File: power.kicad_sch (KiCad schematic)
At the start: 46 parts, among them Q1 CSD18511Q5A, Q2 CSD18511Q5A, Q3 CSD18511Q5A, Q4 CSD18511Q5A, U1 LM25119PSQ/NOPB, U2 DS4432U+, U3 INA260

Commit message: added gerbers and BOM
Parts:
- C1, C3, C4: PARTNO (none) -> 35SVPF82M
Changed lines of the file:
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@@
+			)
+		)
+		(property "PARTNO" "35SVPF82M"
+			(at 57.15 87.63 0)
+			(effects
+				(font
+					(size 1.27 1.27)
+				)
+				(hide yes)
 			)
 		)
@@
 			)
 		)
+		(property "PARTNO" "35SVPF82M"
+			(at 44.45 87.63 0)
+			(effects
+				(font
+					(size 1.27 1.27)
+				)
+				(hide yes)
+			)
+		)
 		(pin "1"
 		)
@@
 			(at 69.85 87.63 0)
 			(effects
+				(font
+					(size 1.27 1.27)
+				)
+				(hide yes)
+			)
+		)
+		(property "PARTNO" "35SVPF82M"
+			(at 69.85 87.63 0)
+			(effects

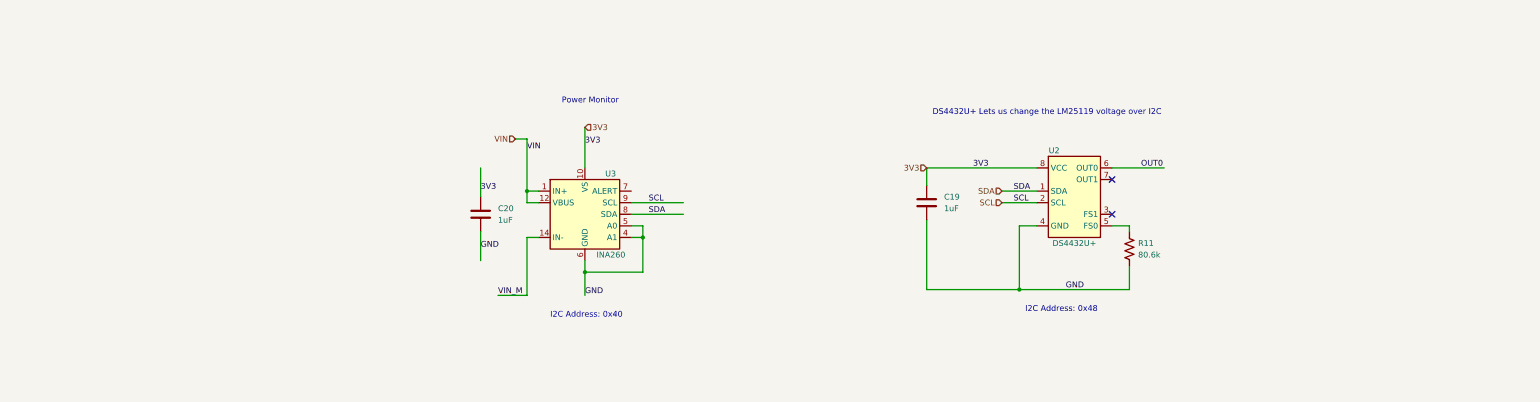
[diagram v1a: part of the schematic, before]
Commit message: added all the ASICs to the schematic. added the RP2040 circuit for data. added the VDDIO boost circuit. schematic cleanup
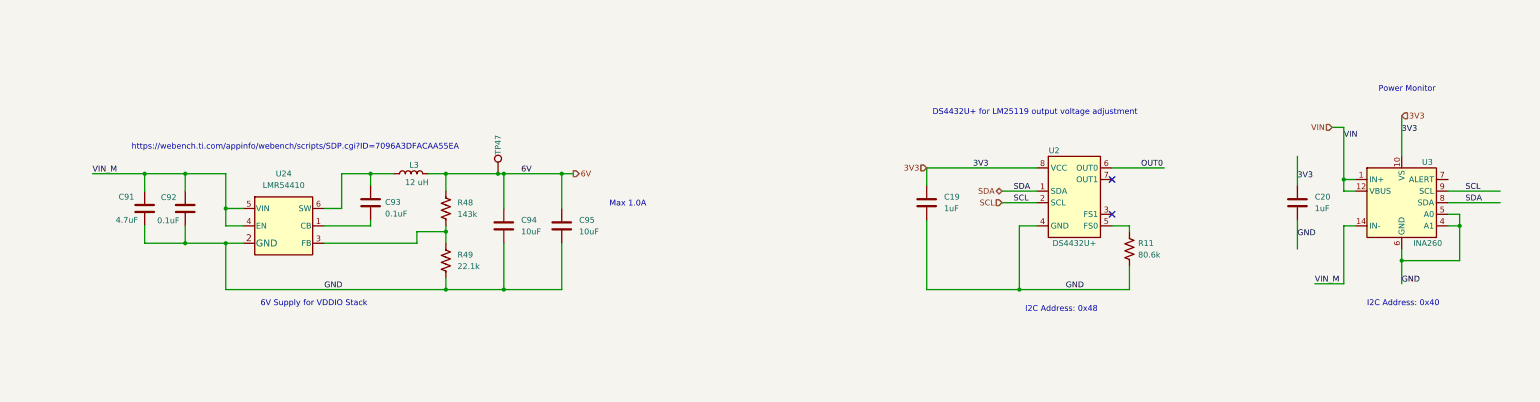
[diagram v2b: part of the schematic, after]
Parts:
- added C91: 4.7uF, Capacitor_SMD:C_0805_2012Metric, symbol Device:C
- added C92: 0.1uF, Capacitor_SMD:C_0603_1608Metric, symbol Device:C
- added C93: 0.1uF, Capacitor_SMD:C_0402_1005Metric, symbol Device:C
- added C94, C95: 10uF, Capacitor_SMD:C_0805_2012Metric, symbol Device:C
- added L3: 12 uH, bitaxe:74438357082, symbol Device:L
- added R48: 143k, Resistor_SMD:R_0402_1005Metric, symbol Device:R_US
- added R49: 22.1k, Resistor_SMD:R_0402_1005Metric, symbol Device:R_US
- added TP47: TestPoint, TestPoint:TestPoint_Pad_D1.0mm, symbol Connector:TestPoint
- added U24: LMR54410, Package_TO_SOT_SMD:SOT-23-6, symbol bitaxe:LMR54410
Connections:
- net GND: now also C91.2, C92.1, C94.2, C95.2, R49.2, U24.2 (GND)
- net VIN_M: now also C91.1, C92.2, U24.4 (EN), U24.5 (VIN)
- new net: C93.2, U24.1 (CB)
- new net: R48.2, R49.1, U24.3 (FB)
- new net: C93.1, L3.1, U24.6 (SW)
- new net 6V: C94.1, C95.1, L3.2, R48.1, TP47.1
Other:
- note added: "6V Supply for VDDIO Stack"
- note added: "DS4432U+ for LM25119 output voltage adjustment"
- note added: "Max 1.0A"
- note added: "https://webench.ti.com/appinfo/webench/scripts/SDP.cgi?ID=7096A3DFACAA55EA"
- note removed: "DS4432U+ Lets us change the LM25119 voltage over I2C"
- moved on the sheet: C20, U3

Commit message: starting layout
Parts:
- L3: footprint bitaxe:74438357082 -> emberone:74438357082
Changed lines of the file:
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@@
 			)
 		)
-		(property "Footprint" "bitaxe:74438357082"
+		(property "Footprint" "emberone:74438357082"
 			(at 138.43 203.2 0)
 			(effects

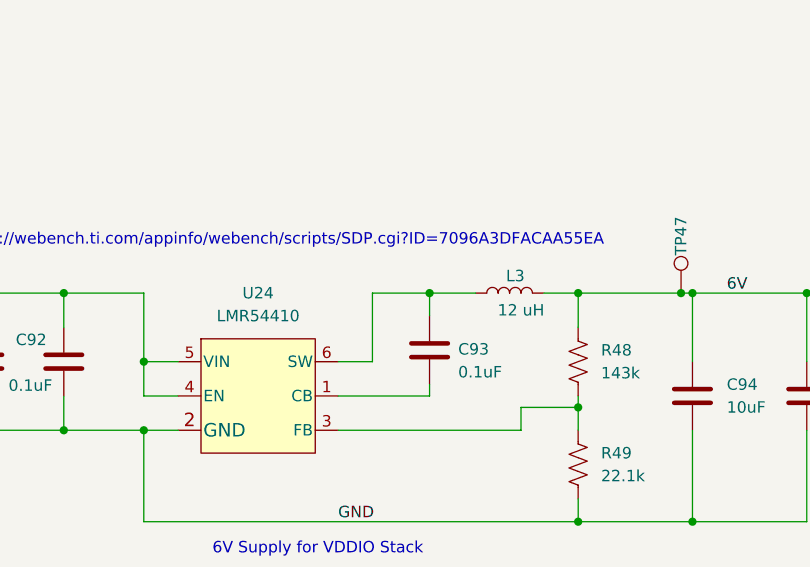
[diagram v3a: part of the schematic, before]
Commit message: moved all the clearance issue passives to the back side and mostly re-routed
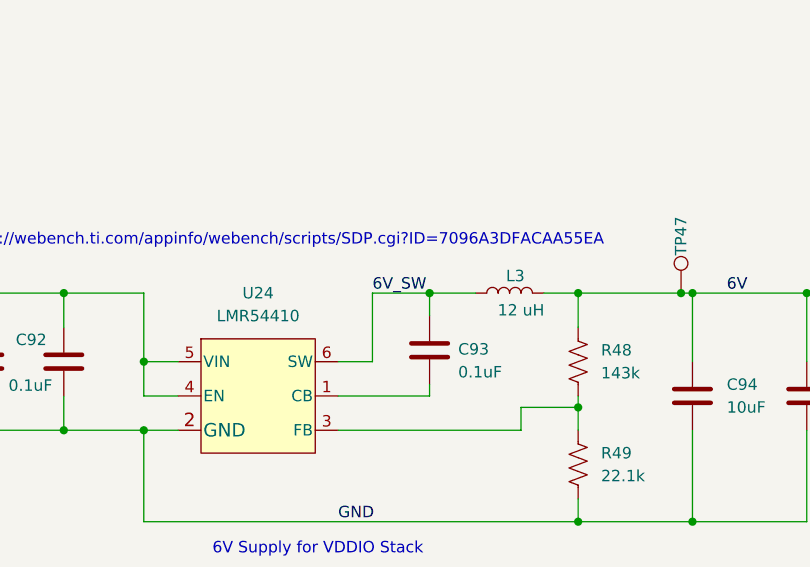
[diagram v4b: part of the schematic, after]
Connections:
- net 6V_SW: now reaches C93.1, L3.1, U24.6 (SW)
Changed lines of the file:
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@@
+		)
+	)
+	(label "6V_SW"
+		(at 123.19 203.2 0)
+		(fields_autoplaced yes)
+		(effects
+			(font
+				(size 1.27 1.27)
+			)
+			(justify left bottom)
 		)
 	)

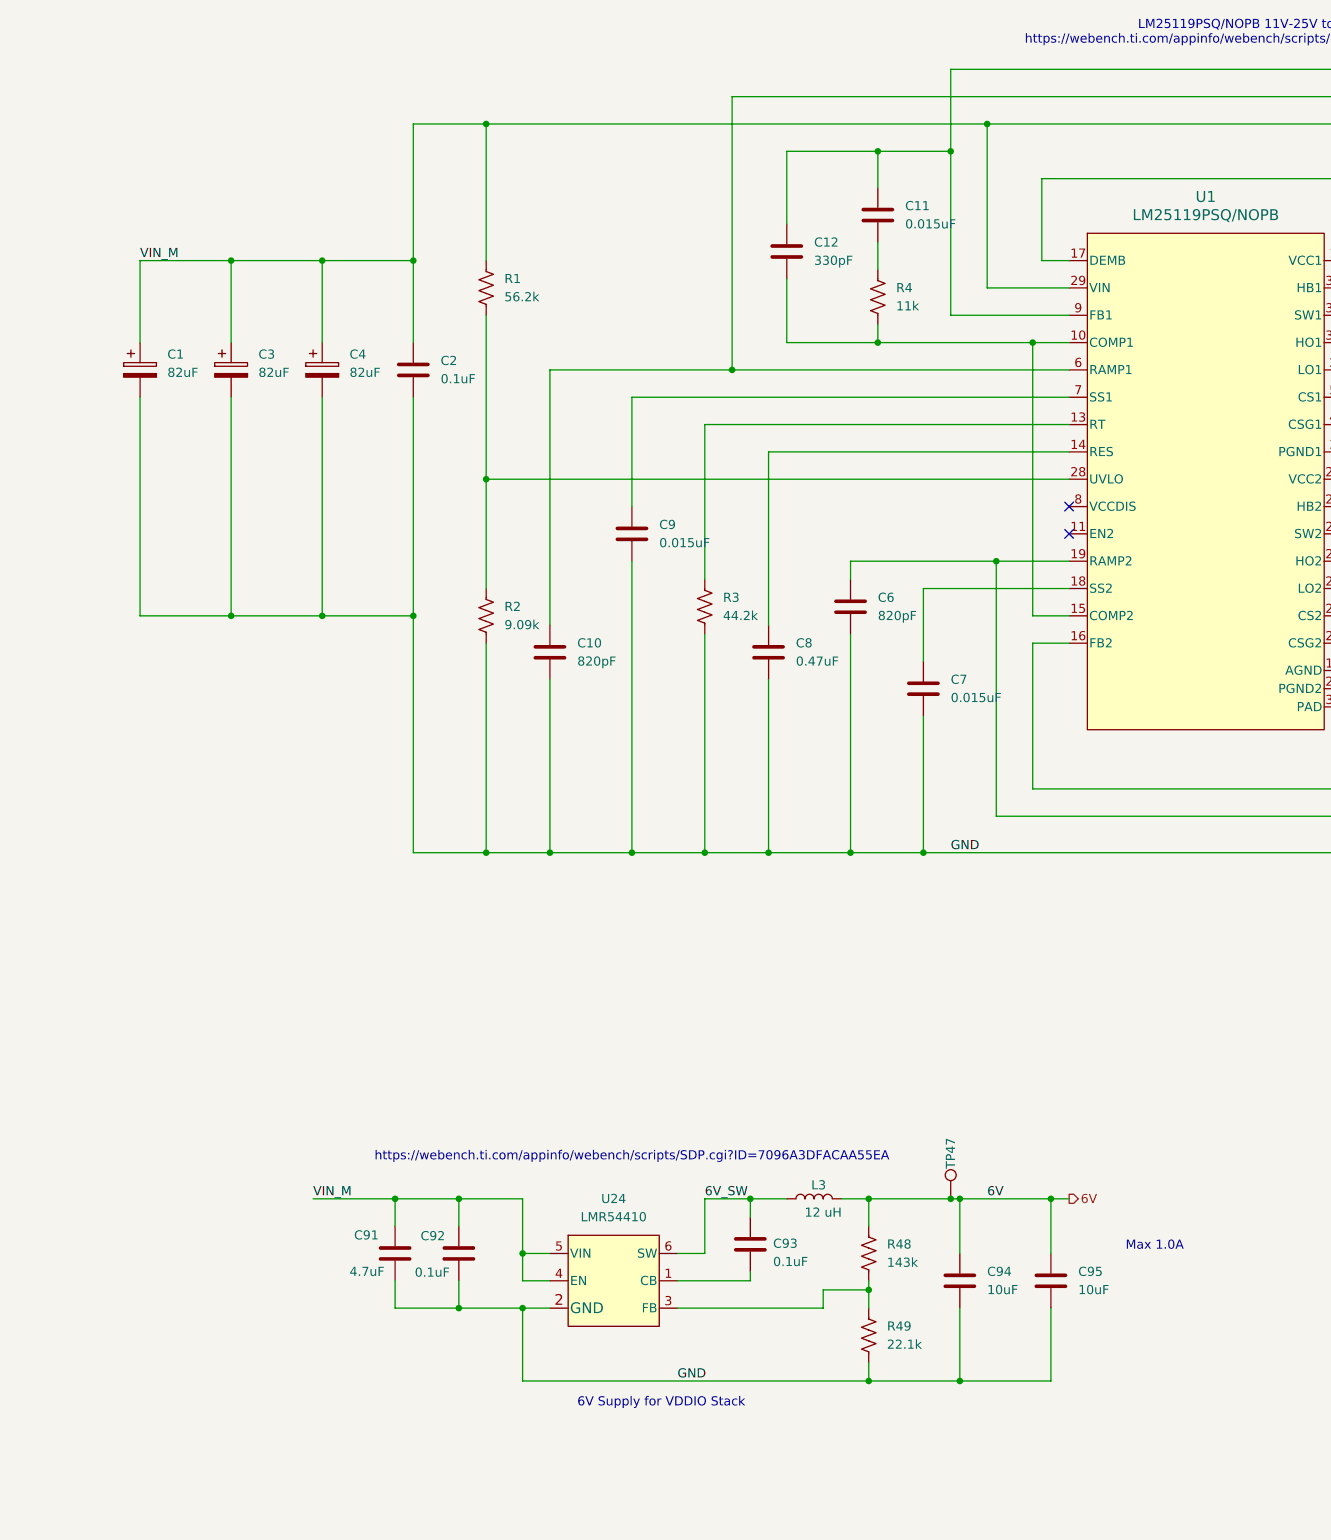
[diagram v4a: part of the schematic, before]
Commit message: added temp sensors. wired up (hopeful) vreg EN circuit. lots of LDO routing.
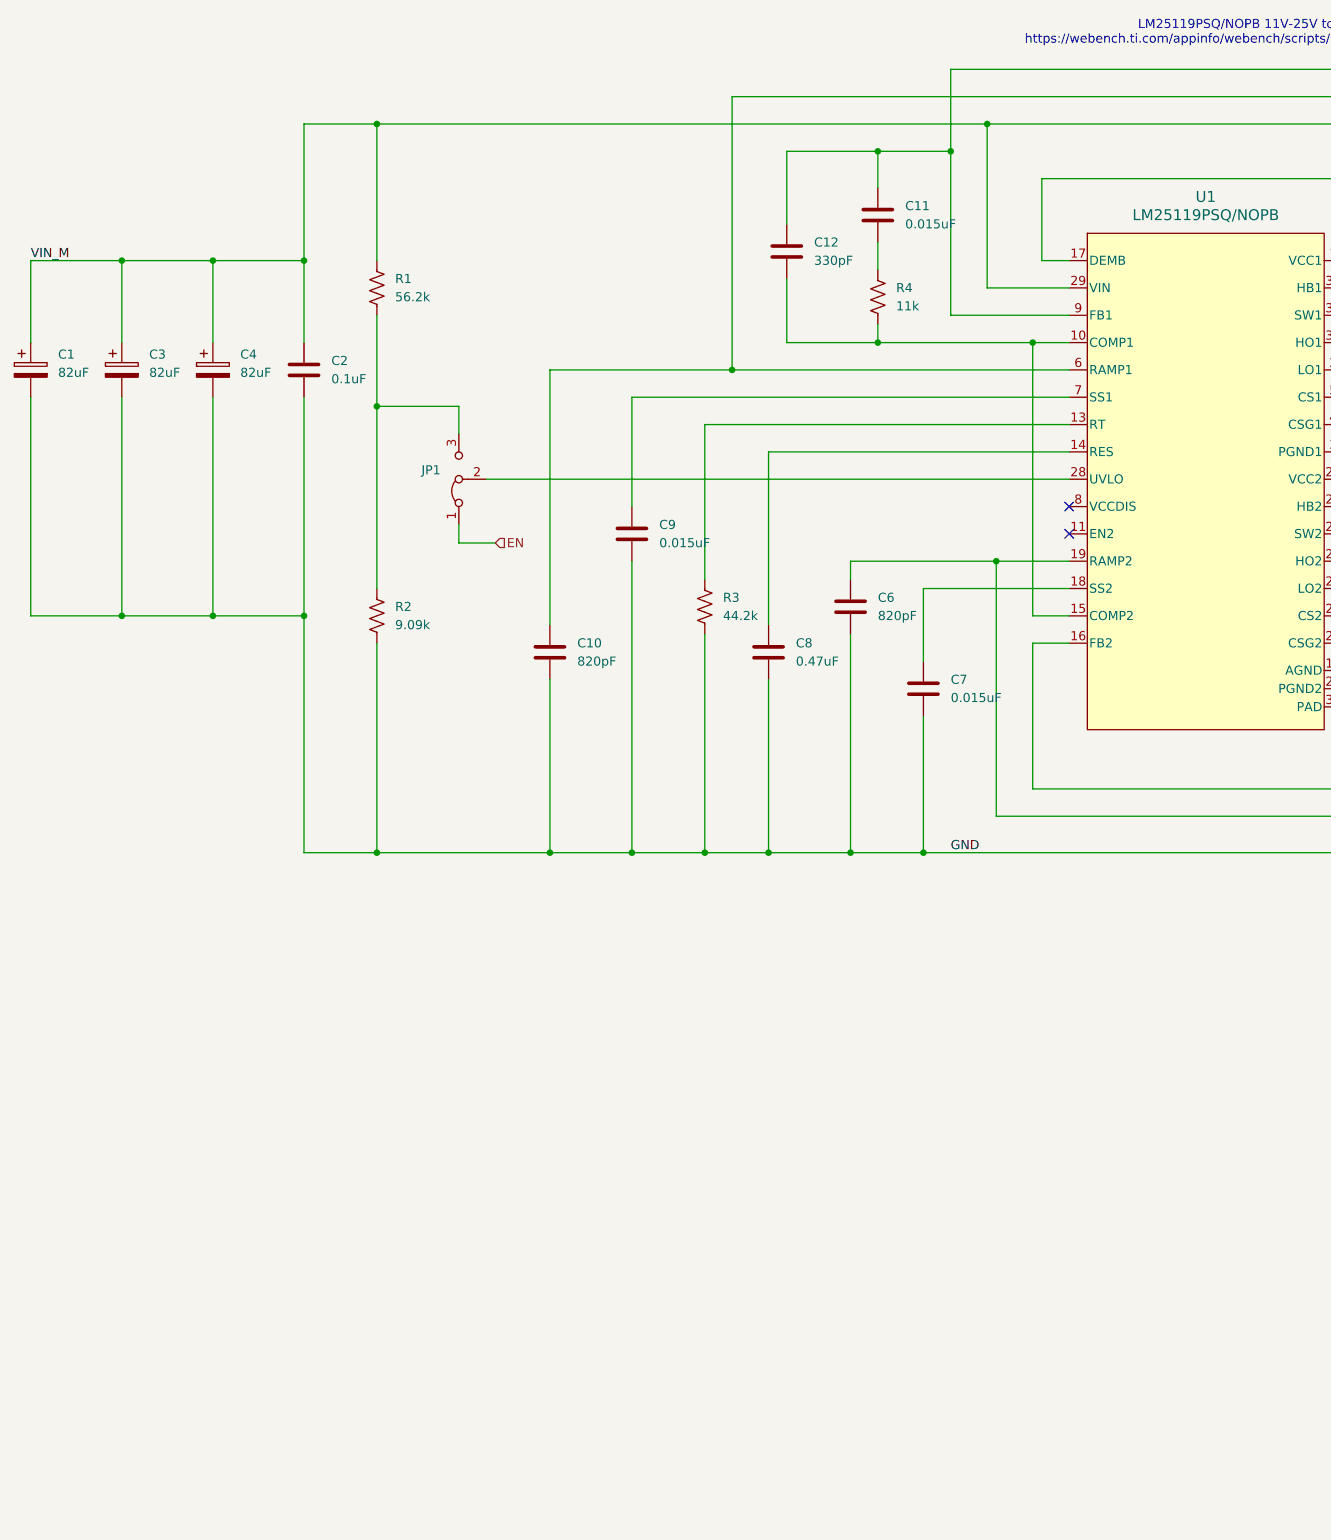
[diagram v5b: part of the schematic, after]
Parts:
- removed C91: 4.7uF, Capacitor_SMD:C_0805_2012Metric, symbol Device:C
- removed C92: 0.1uF, Capacitor_SMD:C_0603_1608Metric, symbol Device:C
- removed C93: 0.1uF, Capacitor_SMD:C_0402_1005Metric, symbol Device:C
- removed C94, C95: 10uF, Capacitor_SMD:C_0805_2012Metric, symbol Device:C
- removed L3: 12 uH, emberone:74438357082, symbol Device:L
- removed R48: 143k, Resistor_SMD:R_0402_1005Metric, symbol Device:R_US
- removed R49: 22.1k, Resistor_SMD:R_0402_1005Metric, symbol Device:R_US
- removed TP47: TestPoint, TestPoint:TestPoint_Pad_D1.0mm, symbol Connector:TestPoint
- removed U24: LMR54410, Package_TO_SOT_SMD:SOT-23-6, symbol bitaxe:LMR54410
- added JP1: Jumper_3_Bridged12, Jumper:SolderJumper-3_P1.3mm_Bridged12_Pad1.0x1.5mm, symbol Jumper:Jumper_3_Bridged12
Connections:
- net at R1.2, R2.1: now also JP1.3 (B); no longer U1.28 (UVLO)
- new net: JP1.2 (C), U1.28 (UVLO)
- new net EN: JP1.1 (A)
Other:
- note removed: "6V Supply for VDDIO Stack"
- note removed: "Max 1.0A"
- note removed: "https://webench.ti.com/appinfo/webench/scripts/SDP.cgi?ID=7096A3DFACAA55EA"
- moved on the sheet: C1, C2, C3, C4, R1, R2

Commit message: generated updated gerbers
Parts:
- removed H1, H2, H3, H4: MountingHole, MountingHole:MountingHole_3.5mm, symbol Mechanical:MountingHole
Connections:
- no-connect marks 4 -> 5

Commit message: updated the partno for C6,C10 for #3 regenerated BOM
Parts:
- C10, C6: DK 311-1194-1-ND -> 399-C0805C821J5GACTUCT-ND; PARTNO CC0805KRX7R9BB821 -> C0805C821J5GACTU
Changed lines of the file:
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@@
 			)
 		)
-		(property "DK" "311-1194-1-ND"
+		(property "DK" "399-C0805C821J5GACTUCT-ND"
 			(at 101.6 127 0)
 			(effects
@@
 			)
 		)
-		(property "PARTNO" "CC0805KRX7R9BB821"
+		(property "PARTNO" "C0805C821J5GACTU"
 			(at 101.6 127 0)
 			(effects
@@
 			)
 		)
-		(property "DK" "311-1194-1-ND"
+		(property "DK" "399-C0805C821J5GACTUCT-ND"
 			(at 143.51 120.65 0)
 			(effects
@@
 			)
 		)
-		(property "PARTNO" "CC0805KRX7R9BB821"
+		(property "PARTNO" "C0805C821J5GACTU"
 			(at 143.51 120.65 0)
 			(effects
